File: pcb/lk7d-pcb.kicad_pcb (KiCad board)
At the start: 2 copper layers, 57.2 x 97.2 mm, 43 parts, among them J1 PINHD_1x4_Male, J2 PINHD_1x4_Male, M1 JLCPCB_2DBarcode_5x5mm, SW1 RotaryEncoder_Switch_MP, SW2 RotaryEncoder_Switch_MP, SW3 SW_Push, SW4 SW_Push, SW5 SW_Push, SW6 SW_Push, SW7 SW_Push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

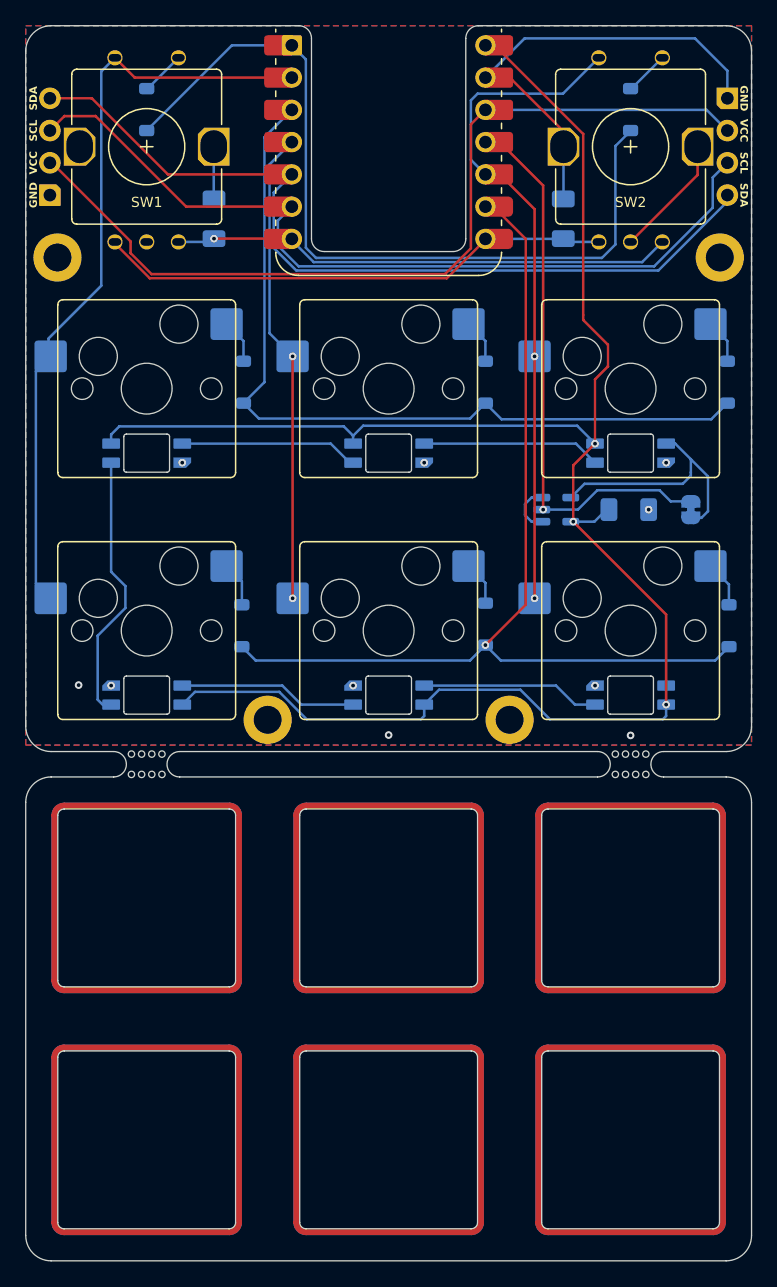
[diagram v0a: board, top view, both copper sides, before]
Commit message: Make the plate a separate PCB
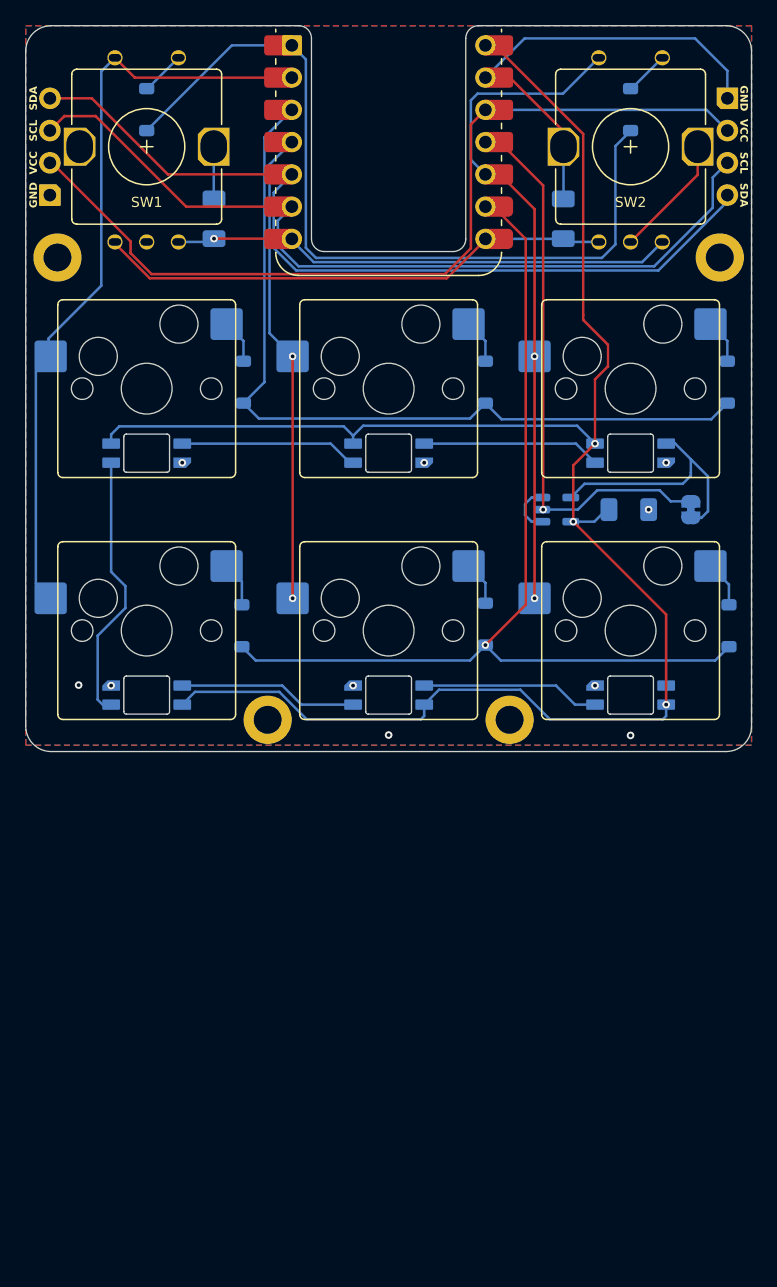
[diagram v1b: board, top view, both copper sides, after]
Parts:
- removed CUT1, CUT2, CUT3, CUT4, CUT5, CUT6: Plate_MX_1U, LKBD_PlateMX:Plate_MX_1U
- removed MB1, MB2: MouseBite_2.0x3.2mm, LKBD_Common:MouseBite_2.0x3.2mm
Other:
- board size 57.2 x 97.2 mm -> 57.2 x 57.2 mm
